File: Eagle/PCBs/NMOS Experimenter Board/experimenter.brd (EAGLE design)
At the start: 83.8 x 99.1 mm, 1526 parts, among them Q100 2N7002, Q101 2N7002, Q102 2N7002, Q103 2N7002, Q104 2N7002, Q105 2N7002, Q106 2N7002, Q107 2N7002, Q108 2N7002, Q109 2N7002, Q110 2N7002, Q111 2N7002, Q112 2N7002, Q113 2N7002, Q114 2N7002, Q115 2N7002, Q116 2N7002, Q117 2N7002, Q118 2N7002, Q119 2N7002, Q120 2N7002, Q2 2N7002, Q25 2N7002, Q26 2N7002, Q27 2N7002, Q28 2N7002, Q29 2N7002, Q3 2N7002, Q30 2N7002, Q31 2N7002, Q32 2N7002, Q33 2N7002, Q34 2N7002, Q35 2N7002, Q36 2N7002, Q37 2N7002, Q38 2N7002, Q39 2N7002, Q4 2N7002, Q40 2N7002, Q41 2N7002, Q42 2N7002, Q43 2N7002, Q44 2N7002, Q45 2N7002, Q46 2N7002, Q47 2N7002, Q48 2N7002, Q49 2N7002, Q5 2N7002, Q50 2N7002, Q51 2N7002, Q52 2N7002, Q53 2N7002, Q54 2N7002, Q55 2N7002, Q56 2N7002, Q57 2N7002, Q58 2N7002, Q59 2N7002, Q6 2N7002, Q60 2N7002, Q61 2N7002, Q62 2N7002, Q63 2N7002, Q64 2N7002, Q65 2N7002, Q66 2N7002, Q67 2N7002, Q68 2N7002, Q69 2N7002, Q7 2N7002, Q70 2N7002, Q71 2N7002, Q72 2N7002, Q73 2N7002, Q74 2N7002, Q75 2N7002, Q76 2N7002, Q77 2N7002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

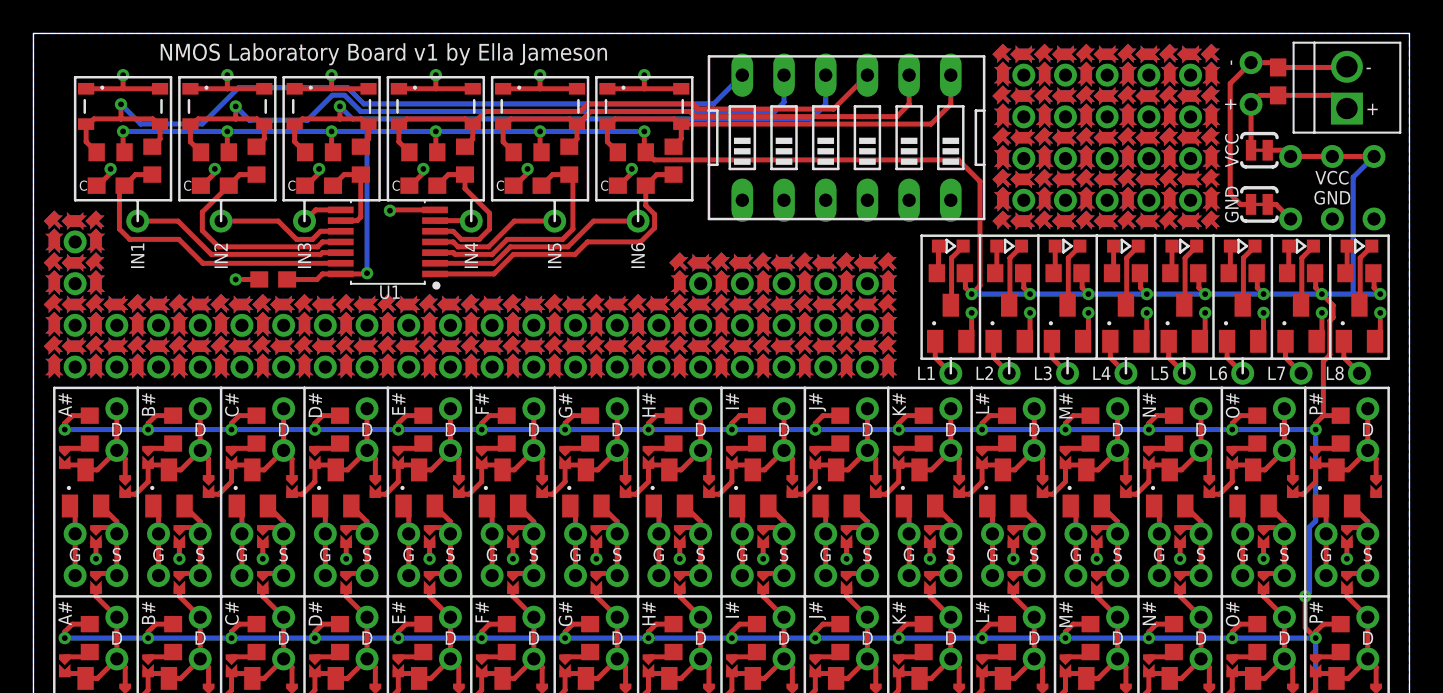
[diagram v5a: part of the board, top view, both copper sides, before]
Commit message: Simplifiied experiment board
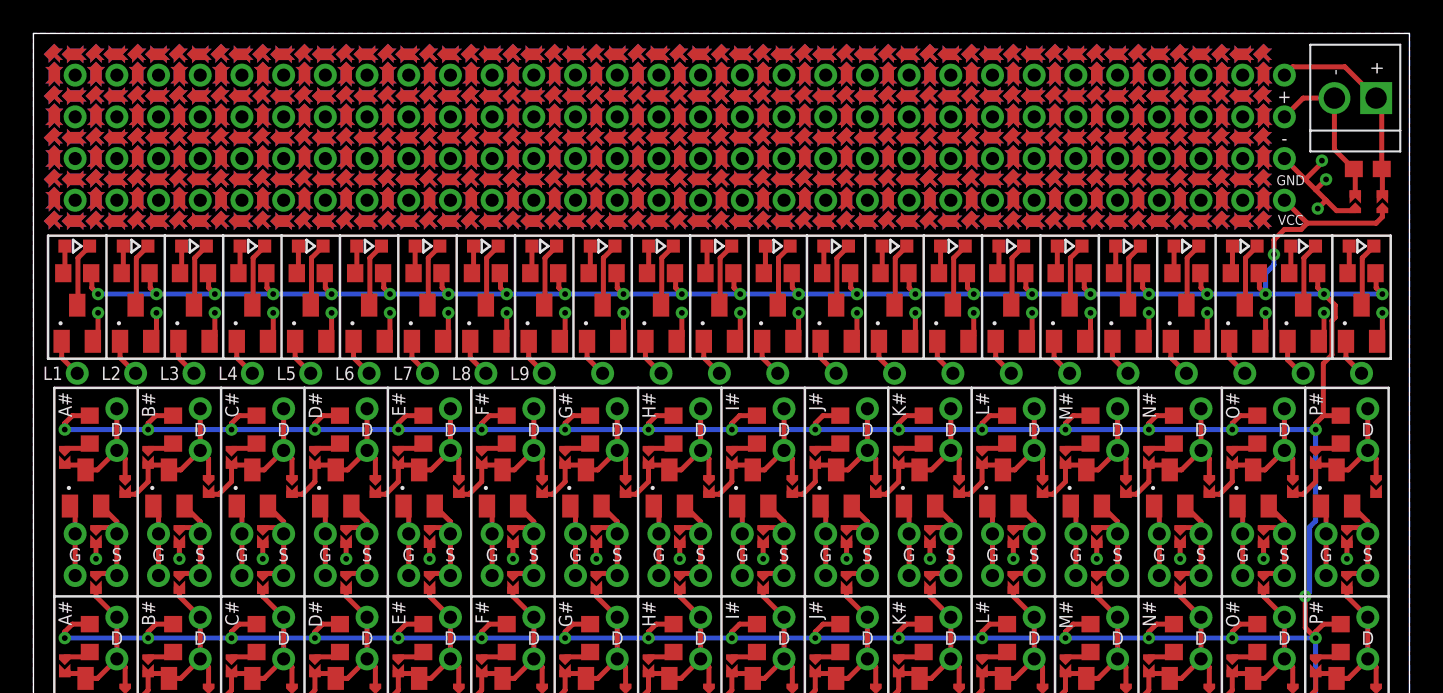
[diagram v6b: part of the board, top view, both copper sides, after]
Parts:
- removed B1, B2, B3, B4, B5, B6, VCC2, VCC3, VSS2, VSS3: TPTHT, ellajameson-core:PROTOPAD-THT-PAD
- removed C1, C11, C2, C3, C5, C7, C9: 0.1u, ellajameson-core:C0603
- removed R75, R76, R77, R78, R81, R82, R85, R86, R89, R90, R93, R94: 10k, ellajameson-core:R0603
- removed S11, S2, S3, S5, S7, S9: (no value), ellajameson-core:SW4_PTS815_SJM_250_SMTR_LFS_CN
- removed SW1: (no value), ellajameson-core:EDG-06
- removed U1: 74HC14PW, ellajameson-core:TSSOP14
- added D10, D11, D12, D13, D14, D15, D16, D17, D18, D19, D20, D21, D22, D23, D24: (no value), ellajameson-core:CHIP-LED0603
- added LED10, LED11, LED12, LED13, LED14, LED15, LED16, LED17, LED18, LED19, LED20, LED21, LED22, LED23, LED24: TPTHT, ellajameson-core:PROTOPAD-THT-PAD
- added Q10, Q11, Q12, Q13, Q14, Q15, Q16, Q17, Q18, Q19, Q20, Q21, Q22, Q23, Q24: 2N7002, ellajameson-core:SOT23
- added R10, R11, R12, R13, R14, R15, R16, R17, R18, R19, R20, R21, R22, R23, R24: 330, ellajameson-core:R0603
- added U$100, U$128, U$132, U$140, U$144, U$148, U$152, U$156, U$160, U$164, U$200, U$284, U$336, U$348, U$352, U$356, U$360, U$364, U$368, U$372, U$376, U$380, U$384, U$388, U$392, U$396, U$400, U$404, U$408, U$412, U$416, U$420, U$424, U$428, U$432, U$436, U$440, U$444, U$448, U$452, U$456, U$460, U$464, U$468, U$472, U$476, U$480, U$484, U$488, U$492, U$496, U$500, U$504, U$508, U$512, U$514, U$516, U$518, U$520, U$522, U$524, U$526, U$528, U$530, U$531: (no value), ellajameson-core:PROTOPAD-CENTER
- added U$101, U$129, U$133, U$141, U$145, U$149, U$153, U$157, U$161, U$165, U$337, U$349, U$353, U$357, U$361, U$365, U$369, U$373, U$377, U$381, U$385, U$389, U$393, U$397, U$401, U$405, U$409, U$413, U$417, U$421, U$425, U$429, U$433, U$437, U$441, U$445, U$449, U$453, U$457, U$461, U$465, U$469, U$473, U$477, U$481, U$485, U$489, U$493, U$497, U$501, U$505, U$509: PROTOPADTHT, ellajameson-core:PROTOPAD-THT
- added U$102, U$103, U$130, U$131, U$138, U$139, U$142, U$143, U$146, U$147, U$150, U$151, U$154, U$155, U$158, U$159, U$162, U$163, U$166, U$167, U$202, U$282, U$334, U$335, U$338, U$339, U$350, U$351, U$354, U$355, U$358, U$359, U$362, U$363, U$366, U$367, U$370, U$371, U$374, U$375, U$378, U$379, U$382, U$383, U$386, U$387, U$390, U$391, U$394, U$395, U$398, U$399, U$402, U$403, U$406, U$407, U$410, U$411, U$414, U$415, U$418, U$419, U$422, U$423, U$426, U$427, U$430, U$431, U$434, U$435, U$438, U$439, U$442, U$443, U$446, U$447, U$450, U$451, U$454, U$455, U$458, U$459, U$462, U$463, U$466, U$467, U$470, U$471, U$474, U$475, U$478, U$479, U$482, U$483, U$486, U$487, U$490, U$491, U$494, U$495, U$498, U$499, U$502, U$503, U$506, U$507, U$510, U$511, U$513, U$515, U$517, U$519, U$521, U$523, U$525, U$527, U$529: (no value), ellajameson-core:PROTOPAD-BETWEEN
- SJ1, SJ2: value SJ_NC -> SJ_NO_THIN; device ellajameson-core:SJ_2S-TRACE -> ellajameson-core:SJ_2S-NO-THIN
- U$104, U$108, U$112, U$116, U$120, U$124, U$168, U$172, U$176, U$180, U$184, U$188, U$192, U$196, U$204, U$340, U$344, U$38, U$42, U$46, U$82, U$86, U$90, U$94: value PROTOPADTHT -> (none); device ellajameson-core:PROTOPAD-THT -> ellajameson-core:PROTOPAD-CENTER
- U$105, U$109, U$113, U$117, U$121, U$125, U$169, U$173, U$177, U$181, U$185, U$189, U$193, U$197, U$201, U$205, U$341, U$345, U$65, U$69: value (none) -> PROTOPADTHT; device ellajameson-core:PROTOPAD-BETWEEN -> ellajameson-core:PROTOPAD-THT
- U$107, U$11, U$111, U$115, U$119, U$123, U$127, U$135, U$171, U$175, U$179, U$183, U$187, U$191, U$195, U$199, U$203, U$343, U$347, U$37, U$41, U$45, U$66, U$70, U$81, U$85, U$89, U$93, U$99: device ellajameson-core:PROTOPAD-CENTER -> ellajameson-core:PROTOPAD-BETWEEN
- U$12, U$136, U$16, U$20, U$208, U$212, U$216, U$220, U$224, U$228, U$232, U$236, U$240, U$244, U$248, U$252, U$256, U$260, U$264, U$268, U$272, U$280, U$288, U$292, U$296, U$300, U$304, U$308, U$312, U$316, U$320, U$324, U$328, U$332, U$36, U$40, U$44, U$48, U$50, U$54, U$58, U$62, U$76, U$80, U$84, U$88, U$92, U$96: device ellajameson-core:PROTOPAD-BETWEEN -> ellajameson-core:PROTOPAD-CENTER
- U$13, U$137, U$17, U$209, U$213, U$217, U$221, U$225, U$229, U$233, U$237, U$241, U$245, U$249, U$253, U$257, U$261, U$265, U$269, U$273, U$277, U$281, U$285, U$289, U$293, U$297, U$301, U$305, U$309, U$313, U$317, U$321, U$325, U$329, U$33, U$333, U$73, U$77, U$9, U$97: value (none) -> PROTOPADTHT; device ellajameson-core:PROTOPAD-CENTER -> ellajameson-core:PROTOPAD-THT
- U$14, U$18, U$206, U$210, U$214, U$218, U$222, U$226, U$230, U$234, U$238, U$242, U$246, U$250, U$254, U$258, U$262, U$266, U$270, U$278, U$286, U$290, U$294, U$298, U$302, U$306, U$310, U$314, U$318, U$322, U$326, U$330, U$34, U$49, U$53, U$57, U$61, U$74, U$78: value PROTOPADTHT -> (none); device ellajameson-core:PROTOPAD-THT -> ellajameson-core:PROTOPAD-BETWEEN
- moved U$99 69.6 mm to (2.54, 95.2), turned to 90 degrees
- moved U$98 67.0 mm to (3.81, 94.0), turned to 0 degrees
- moved U$97 66.7 mm to (2.54, 94.0)
- moved U$37 64.3 mm to (7.62, 87.6), turned to 90 degrees
- moved U$75 61.7 mm to (7.62, 92.7), turned to 90 degrees
- moved U$79 61.7 mm to (10.2, 92.7), turned to 90 degrees
- moved U$77 59.4 mm to (10.2, 91.4)
- moved U$73 59.4 mm to (7.62, 91.4)
- moved U$74 59.3 mm to (8.89, 91.4)
- moved U$76 59.3 mm to (8.89, 92.7), turned to 0 degrees
- moved U$78 59.1 mm to (11.4, 91.4)
- moved U$80 59.1 mm to (11.4, 92.7), turned to 0 degrees
- moved U$1 58.0 mm to (2.54, 88.9)
- moved U$21 58.0 mm to (5.08, 88.9)
- moved U$22 58.0 mm to (6.35, 88.9)
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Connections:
- removed net N$294: C3.1, R78.1, U1.11
- removed net N$295: B4.P1, U1.6
- removed net N$296: B3.P1, U1.8
- removed net N$298: C5.1, R82.1, U1.9
- removed net N$299: B2.P1, U1.10
- removed net N$300: B1.P1, U1.12
- removed net N$302: C7.1, R86.1, U1.5
- removed net N$306: C9.1, R90.1, U1.3
- removed net N$310: C11.1, R94.1, U1.1
- removed net N$5: B6.P1, U1.2
- removed net N$8: C2.1, R76.1, U1.13
- removed net S1G: R75.1, R76.2, S2.3, S2.4, SW1.12
- removed net S2G: R77.1, R78.2, S3.3, S3.4, SW1.11
- removed net S3G: R81.1, R82.2, S5.3, S5.4, SW1.10
- removed net S4G: R85.1, R86.2, S7.3, S7.4, SW1.9
- removed net S5G: R89.1, R90.2, S9.3, S9.4, SW1.8
- removed net S6G: R93.1, R94.2, S11.3, S11.4, SW1.7
- new net N$2: D10.A, R10.1
- new net N$3: LED10.P1, Q10.1
- new net N$31: D11.A, R11.1
- new net N$32: LED11.P1, Q11.1
- new net N$33: D11.C, Q11.3
- new net N$34: D12.A, R12.1
- new net N$35: LED12.P1, Q12.1
- new net N$36: D12.C, Q12.3
- new net N$37: D13.A, R13.1
- new net N$38: LED13.P1, Q13.1
- new net N$39: D13.C, Q13.3
- new net N$40: D14.A, R14.1
- new net N$41: LED14.P1, Q14.1
- new net N$42: D14.C, Q14.3
- new net N$43: D15.A, R15.1
- new net N$44: LED15.P1, Q15.1
- new net N$45: D15.C, Q15.3
- new net N$46: D16.A, R16.1
- new net N$47: LED16.P1, Q16.1
- new net N$48: D16.C, Q16.3
- new net N$49: D17.A, R17.1
- new net N$50: LED17.P1, Q17.1
- new net N$51: D17.C, Q17.3
- new net N$52: D18.A, R18.1
- new net N$53: LED18.P1, Q18.1
- new net N$54: D18.C, Q18.3
- new net N$55: D19.A, R19.1
- new net N$56: LED19.P1, Q19.1
- new net N$57: D19.C, Q19.3
- new net N$58: D20.A, R20.1
- new net N$59: LED20.P1, Q20.1
- new net N$60: D20.C, Q20.3
- new net N$61: D21.A, R21.1
- new net N$62: LED21.P1, Q21.1
- new net N$63: D21.C, Q21.3
- new net N$64: D22.A, R22.1
- new net N$65: LED22.P1, Q22.1
- new net N$66: D22.C, Q22.3
- new net N$67: D23.A, R23.1
- new net N$68: LED23.P1, Q23.1
- new net N$69: D23.C, Q23.3
- new net N$70: D24.A, R24.1
- new net N$71: LED24.P1, Q24.1
- new net N$72: D24.C, Q24.3
- net GND: now also Q10.2, Q11.2, Q12.2, Q13.2, Q14.2, Q15.2, Q16.2, Q17.2, Q18.2, Q19.2, Q20.2, Q21.2, Q22.2, Q23.2, Q24.2; no longer C1.2, C11.2, C2.2, C3.2, C5.2, C7.2, C9.2, S11.1, S11.2, S2.1, S2.2, S3.1, S3.2, S5.1, S5.2, S7.1, S7.2, S9.1, S9.2, SW1.1, SW1.2, SW1.3, SW1.4, SW1.5, SW1.6, U1.7, VSS2.P1, VSS3.P1
- net N$6: now also D10.C, Q10.3; no longer B5.P1, U1.4
- net VCC: now also R10.2, R11.2, R12.2, R13.2, R14.2, R15.2, R16.2, R17.2, R18.2, R19.2, R20.2, R21.2, R22.2, R23.2, R24.2; no longer C1.1, R75.2, R77.2, R81.2, R85.2, R89.2, R93.2, U1.14, VCC2.P1, VCC3.P1
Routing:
- net S1G: track 49.6 -> 0.00 mm, vias 1 -> 0
- net S2G: track 45.7 -> 0.00 mm, vias 1 -> 0
- net S3G: track 41.1 -> 0.00 mm, vias 1 -> 0
- net S4G: track 33.8 -> 0.00 mm
- net S5G: track 31.1 -> 0.00 mm
- net S6G: track 27.0 -> 0.00 mm
- net N$310: track 19.3 -> 0.00 mm
- net N$8: track 19.1 -> 0.00 mm
- net N$306: track 14.5 -> 0.00 mm
- net N$294: track 14.3 -> 0.00 mm
- net N$5: track 13.4 -> 0.00 mm
- net N$300: track 13.3 -> 0.00 mm
- net N$302: track 9.69 -> 0.00 mm
- net GND: track 146.7 -> 137.1 mm, vias 118 -> 122
- net VCC: track 866.2 -> 857.3 mm, vias 116 -> 125
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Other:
- board text added: "L9"
- board text added: "NMOS Laboratory Board v1"
- board text added: "by Ella Jameson (ellagjameson@gmail.com)"
- board text removed: "C"
- board text removed: "IN1"
- board text removed: "IN2"
- board text removed: "IN3"
- board text removed: "IN4"
- board text removed: "IN5"
- board text removed: "IN6"
- board text removed: "NMOS Laboratory Board v1 by Ella Jameson"
